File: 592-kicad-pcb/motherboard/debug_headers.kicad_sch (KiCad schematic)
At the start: 7 parts, among them J10 Conn_02x06_Odd_Even, J11 Conn_02x06_Odd_Even, J12 Conn_02x06_Odd_Even, J13 Conn_02x06_Odd_Even, J7 Conn_02x06_Odd_Even, J8 Conn_02x06_Odd_Even, J9 Conn_02x06_Odd_Even

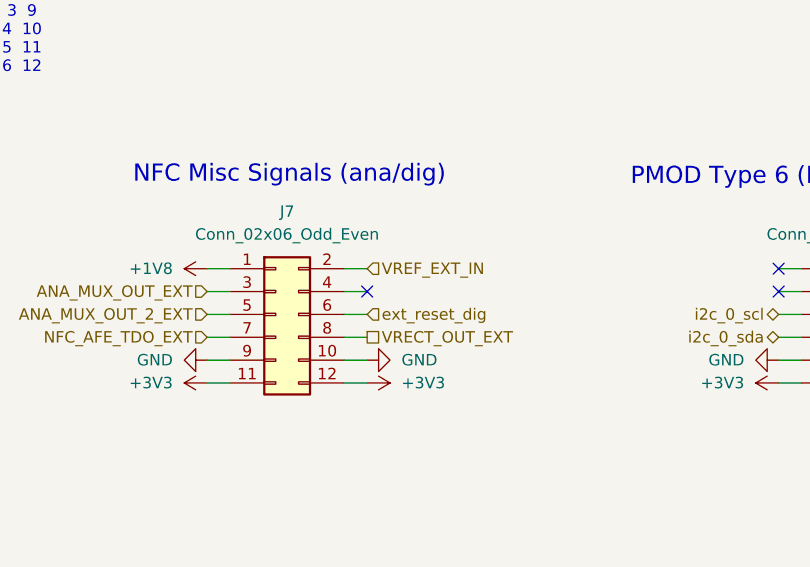
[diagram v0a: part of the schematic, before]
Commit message: partial update to use STM board, updated muxing of FTDI
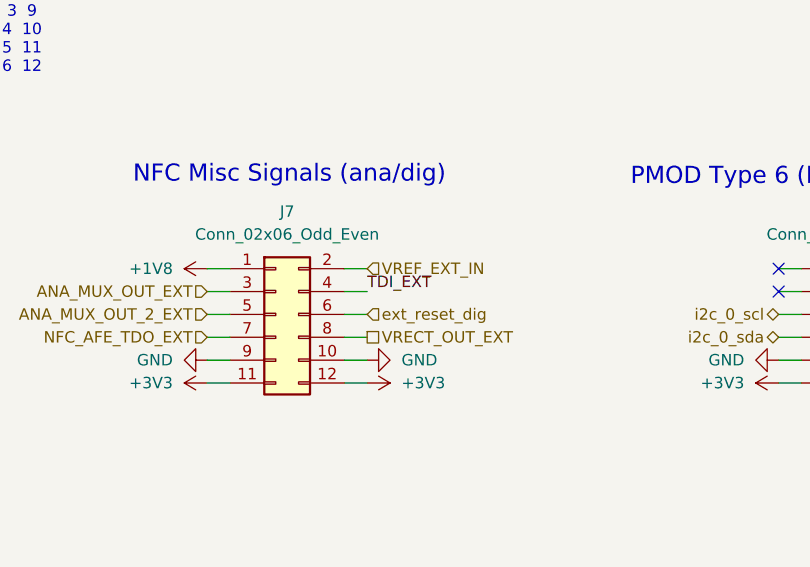
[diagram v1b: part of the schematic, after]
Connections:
- net TDI_EXT: now also J7.4 (Pin_4)
- no-connect marks 18 -> 17
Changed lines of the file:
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@@
-	)
-	(no_connect
-		(at 62.23 54.61)
 	)
 	(no_connect
@@
 		)
 	)
+	(label "TDI_EXT"
+		(at 62.23 54.61 0)
+		(effects
+			(font
+				(size 1.27 1.27)
+			)
+			(justify left bottom)
+		)
+	)

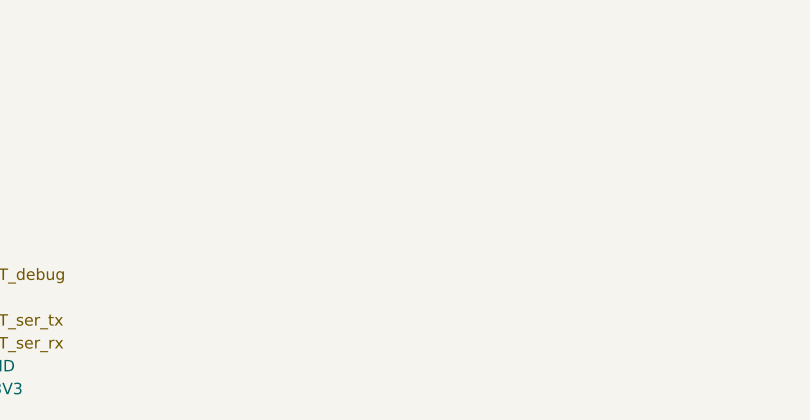
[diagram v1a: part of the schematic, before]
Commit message: update FTDI interfacing
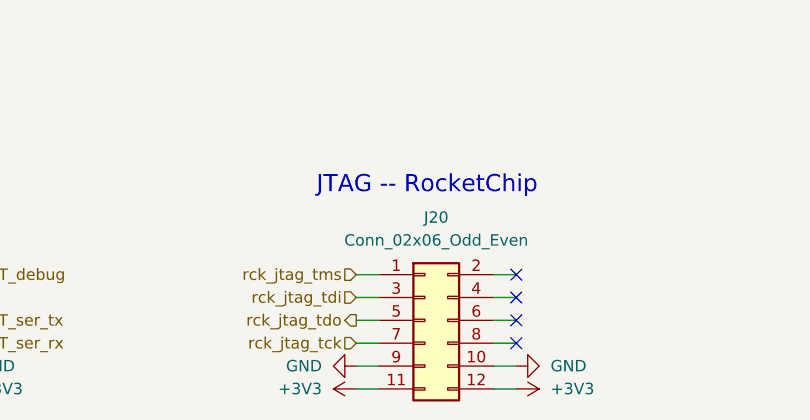
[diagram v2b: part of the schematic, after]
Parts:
- added J20: Conn_02x06_Odd_Even, Connector_PinSocket_2.54mm:PinSocket_2x06_P2.54mm_Horizontal, symbol Connector_Generic:Conn_02x06_Odd_Even
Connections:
- net +3V3: now also J20.11 (Pin_11), J20.12 (Pin_12)
- net GND: now also J20.10 (Pin_10), J20.9 (Pin_9)
- new net rck_jtag_tck: J20.7 (Pin_7)
- new net rck_jtag_tdi: J20.3 (Pin_3)
- new net rck_jtag_tdo: J20.5 (Pin_5)
- new net rck_jtag_tms: J20.1 (Pin_1)
- no-connect marks 17 -> 21
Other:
- note added: "JTAG -- RocketChip"

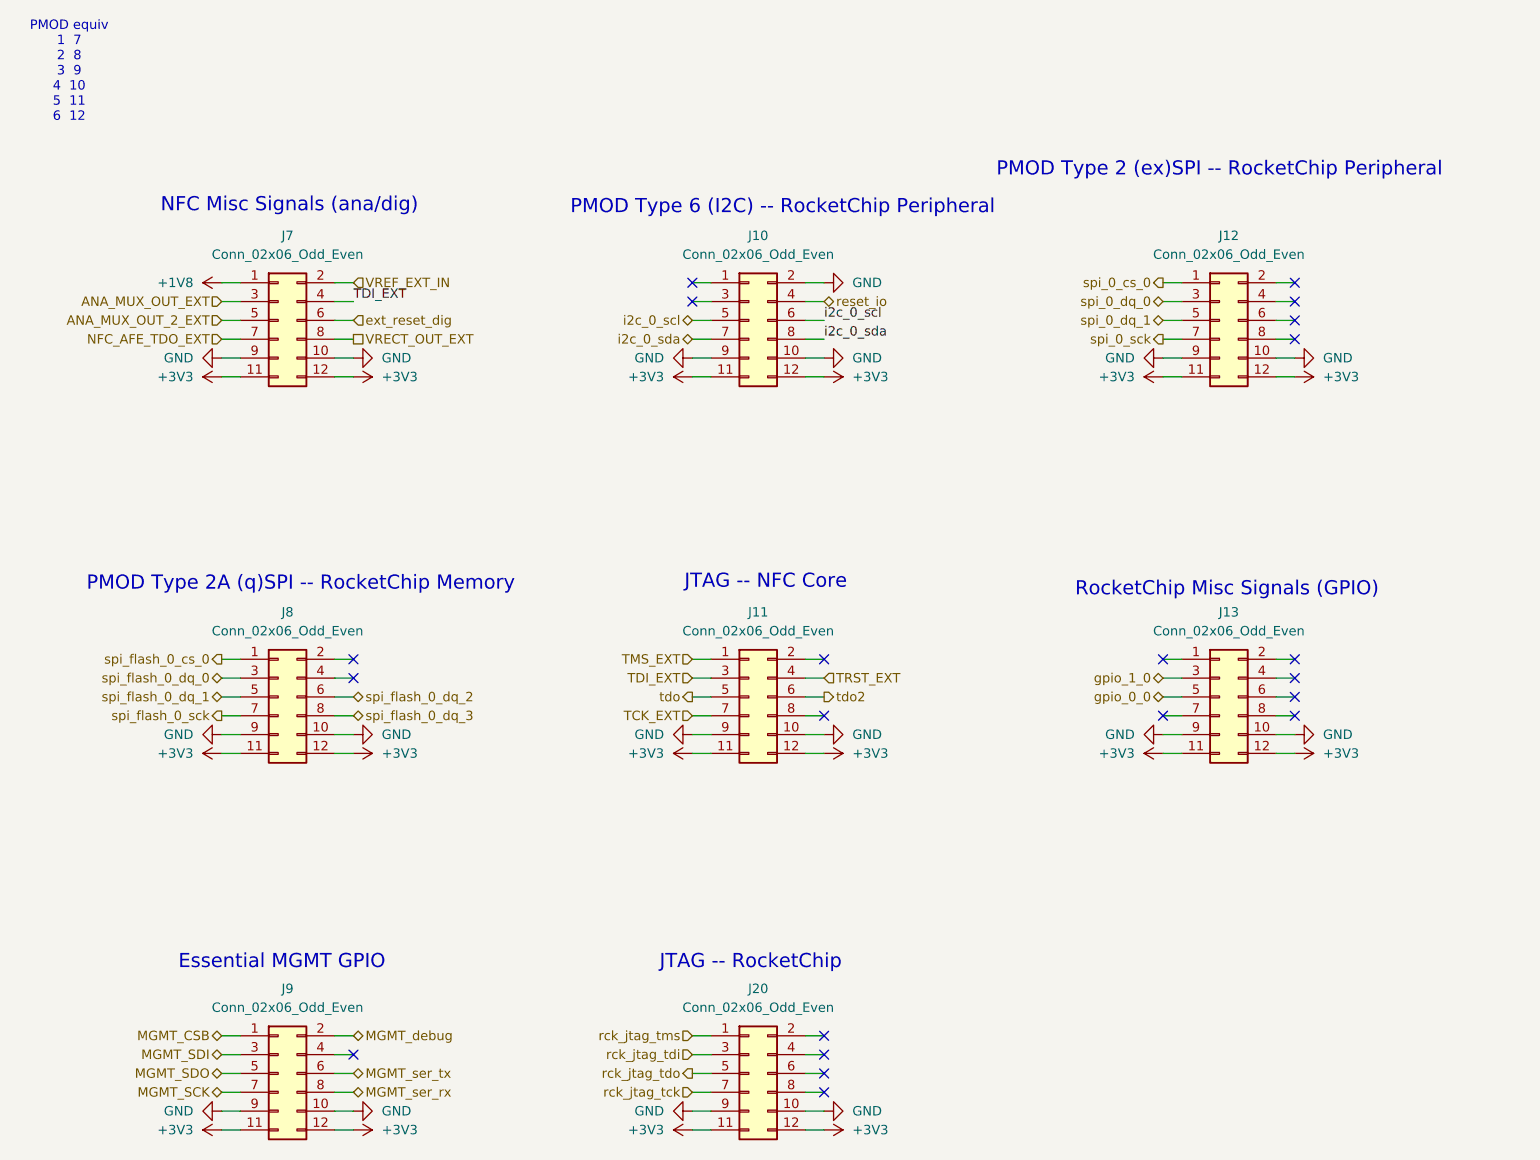
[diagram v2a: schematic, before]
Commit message: add JLC part num for parts, footprints
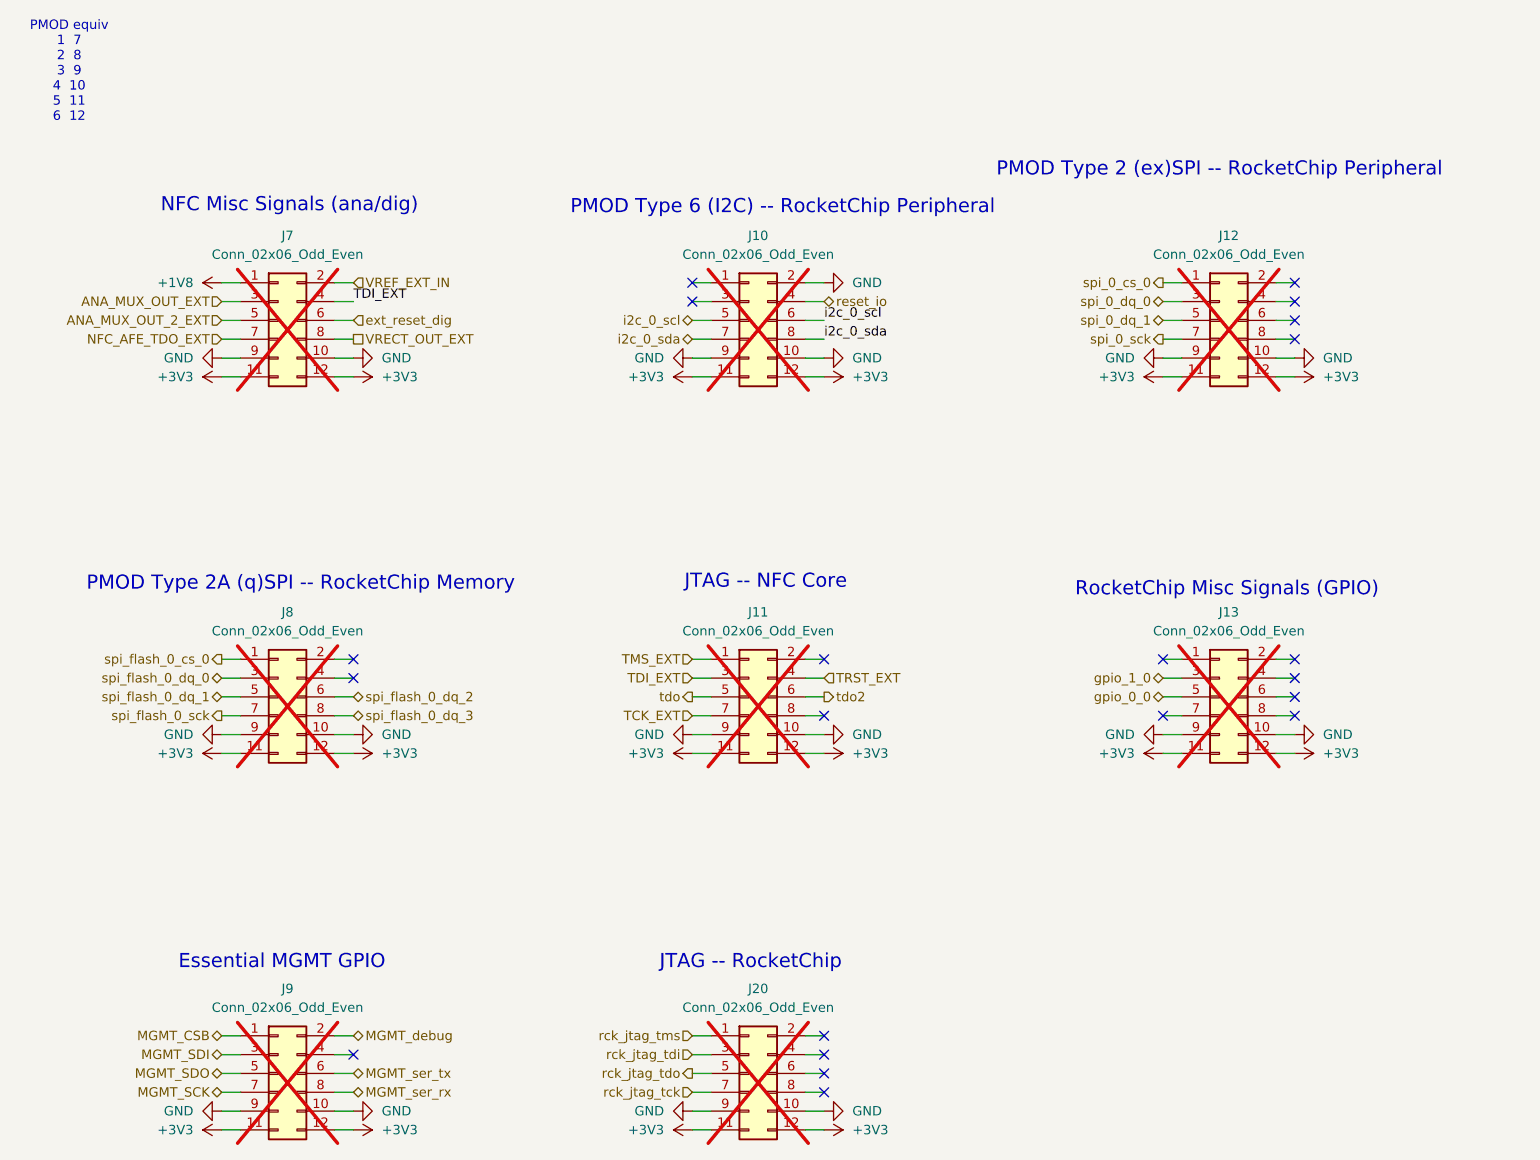
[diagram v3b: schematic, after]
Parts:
- J10, J11, J12, J13, J20, J7, J8, J9: now not fitted
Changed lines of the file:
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@@
 		(in_bom yes)
 		(on_board yes)
-		(dnp no)
+		(dnp yes)
 		(fields_autoplaced yes)
 		(property "Reference" "J20"
@@
 		(in_bom yes)
 		(on_board yes)
-		(dnp no)
+		(dnp yes)
 		(fields_autoplaced yes)
 		(property "Reference" "J8"
@@
 		(in_bom yes)
 		(on_board yes)
-		(dnp no)
+		(dnp yes)
 		(fields_autoplaced yes)
 		(property "Reference" "J9"
@@
 		(in_bom yes)
 		(on_board yes)
-		(dnp no)
+		(dnp yes)
 		(fields_autoplaced yes)
 		(property "Reference" "J11"
@@
 		(in_bom yes)
 		(on_board yes)
-		(dnp no)
+		(dnp yes)
 		(fields_autoplaced yes)
 		(property "Reference" "J12"
@@
 		(in_bom yes)
 		(on_board yes)
-		(dnp no)
+		(dnp yes)
 		(fields_autoplaced yes)
 		(property "Reference" "J7"
@@
 		(in_bom yes)
 		(on_board yes)
-		(dnp no)
+		(dnp yes)
 		(fields_autoplaced yes)
 		(property "Reference" "J13"
@@
 		(in_bom yes)
 		(on_board yes)
-		(dnp no)
+		(dnp yes)
 		(fields_autoplaced yes)
 		(property "Reference" "J10"

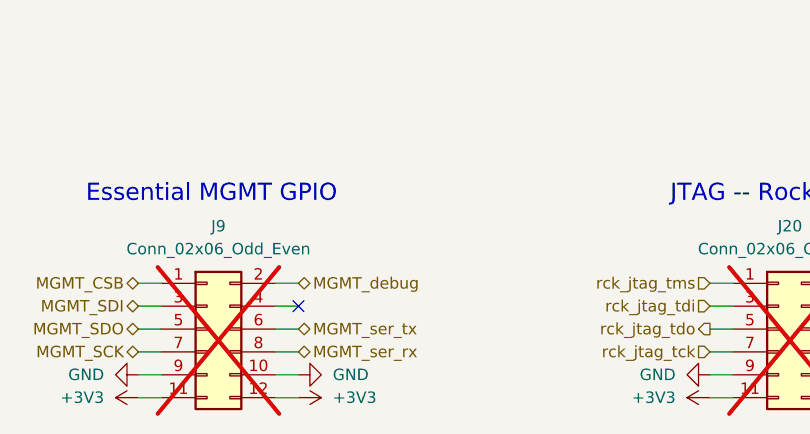
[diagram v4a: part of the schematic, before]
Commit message: map to STM pins
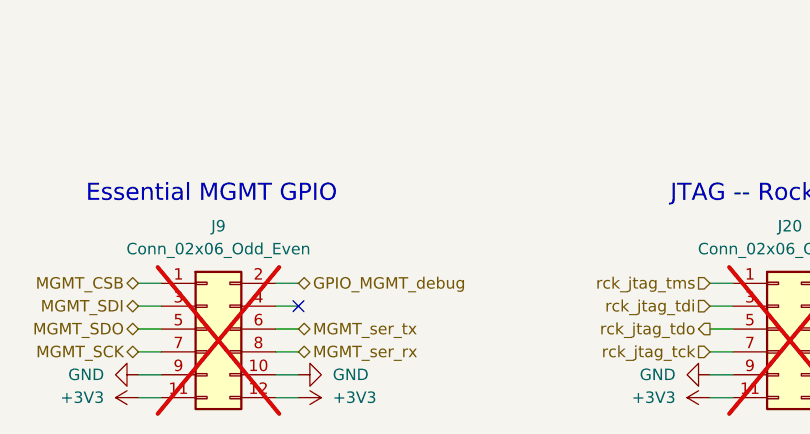
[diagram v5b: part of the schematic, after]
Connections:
- net MGMT_debug renamed GPIO_MGMT_debug
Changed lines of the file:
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@@
 		)
 	)
-	(hierarchical_label "MGMT_debug"
+	(hierarchical_label "GPIO_MGMT_debug"
 		(shape bidirectional)
 		(at 62.23 153.67 0)

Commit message: updates to routing
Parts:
- renumbered J7 to J10, J8 to J11, J9 to J12, J10 to J13, J11 to J14, J20 to J15, J12 to J16, J13 to J17
